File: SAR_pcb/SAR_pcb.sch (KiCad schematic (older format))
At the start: 41 parts, among them J1 Conn_Coaxial_Power, J10 Conn_Coaxial, J11 Conn_Coaxial, J12 Conn_01x02, J13 Conn_01x02, J14 Conn_01x02, J15 Conn_01x02, J16 Conn_01x02, J17 Conn_01x02, J18 Conn_01x02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

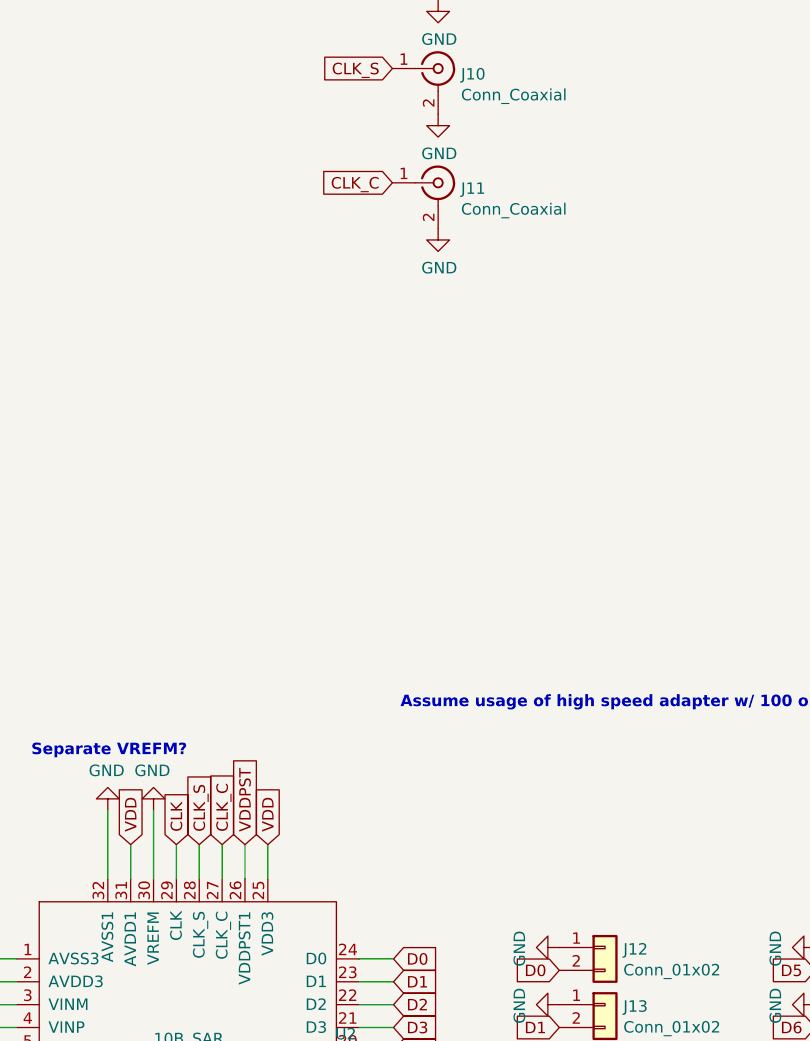
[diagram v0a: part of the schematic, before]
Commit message: Added jumper resistance for feeding clk_c
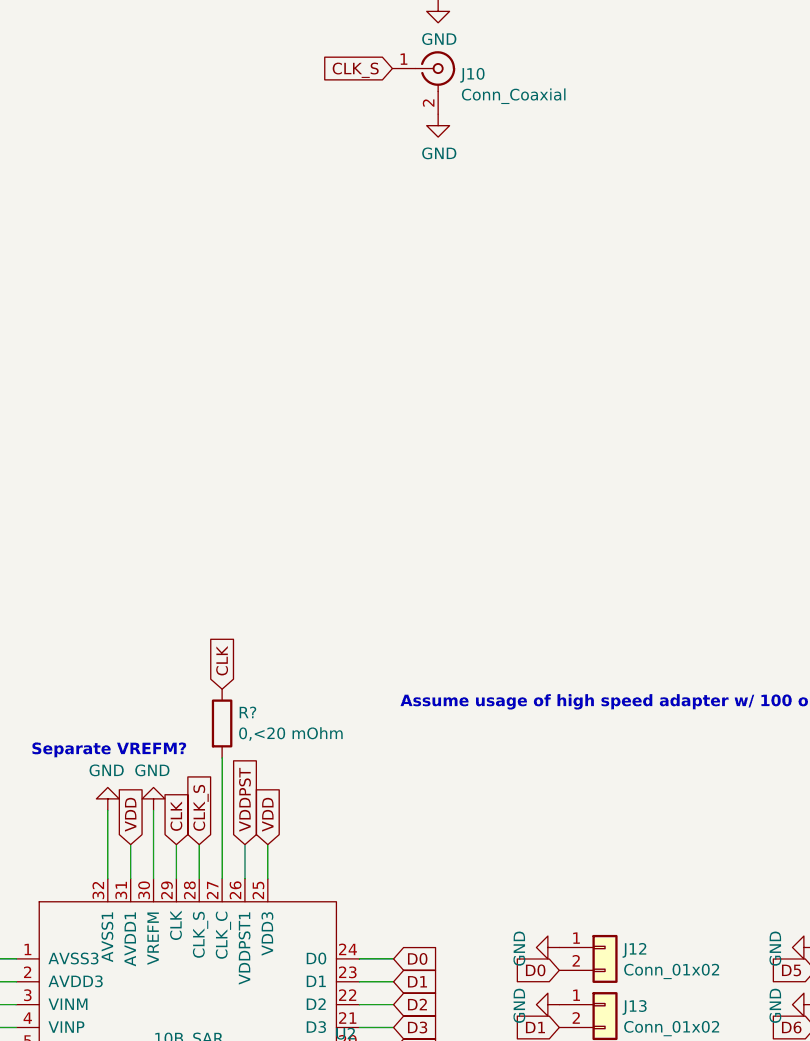
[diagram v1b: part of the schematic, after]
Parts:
- removed J11: Conn_Coaxial, Connector_Coaxial:SMA_Amphenol_132289_EdgeMount, symbol Connector:Conn_Coaxial
- added R?: 0,<20 mOhm, Resistor_SMD:R_0805_2012Metric, symbol Device:R
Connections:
- net CLK: now also R?.1
- net CLK_C: no longer names the net of U2.27 (CLK_C)
- net CLK_C: now also R?.2
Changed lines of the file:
@@
 Comment4 ""
 $EndDescr
-Text GLabel 6005 4745 1    50   Input ~ 0
-CLK_C
 Text GLabel 6105 4745 1    50   Input ~ 0
 VDDPST
@@
 	6105 4895 6105 4745
 Wire Wire Line
-	6005 4895 6005 4745
-Wire Wire Line
 	5905 4895 5905 4745
 Wire Wire Line
@@
 $EndComp
 $Comp
-L Connector:Conn_Coaxial J11
-U 1 1 5F7C18E6
-P 6950 1850
-F 0 "J11" H 7050 1825 50  0000 L CNN
-F 1 "Conn_Coaxial" H 7050 1734 50  0000 L CNN
-F 2 "Connector_Coaxial:SMA_Amphenol_132289_EdgeMount" H 6950 1850 50  0001 C CNN
-F 3 " ~" H 6950 1850 50  0001 C CNN
-	1    6950 1850
-	1    0    0    -1
-$EndComp
-$Comp
 L Connector:Conn_Coaxial J9
 U 1 1 5F7C2E44
@@
 $EndComp
 $Comp
-L power:GND #PWR019
-U 1 1 5F7C5123
-P 6950 2050
-F 0 "#PWR019" H 6950 1800 50  0001 C CNN
-F 1 "GND" H 6955 1877 50  0000 C CNN
-F 2 "" H 6950 2050 50  0001 C CNN
-F 3 "" H 6950 2050 50  0001 C CNN
-	1    6950 2050
-	1    0    0    -1
-$EndComp
-$Comp
 L power:GND #PWR018
 U 1 1 5F7C6414
@@
 	1    0    0    -1
 $EndComp
-Text GLabel 6750 1850 0    50   Input ~ 0
-CLK_C
 Text GLabel 6750 1350 0    50   Input ~ 0
 CLK_S
@@
 EndData
 $EndBitmap
+Text GLabel 6005 4065 1    50   Input ~ 0
+CLK
+$Comp
+L Device:R R?
+U 1 1 5F8560B6
+P 6005 4215
+F 0 "R?" H 6075 4261 50  0000 L CNN
+F 1 "0,<20 mOhm" H 6075 4170 50  0000 L CNN
+F 2 "Resistor_SMD:R_0805_2012Metric" V 5935 4215 50  0001 C CNN
+F 3 "https://www.digikey.com/short/znt8qf" H 6005 4215 50  0001 C CNN
+	1    6005 4215
+	1    0    0    -1
+$EndComp
+Wire Wire Line
+	6005 4365 6005 4895
 $EndSCHEMATC

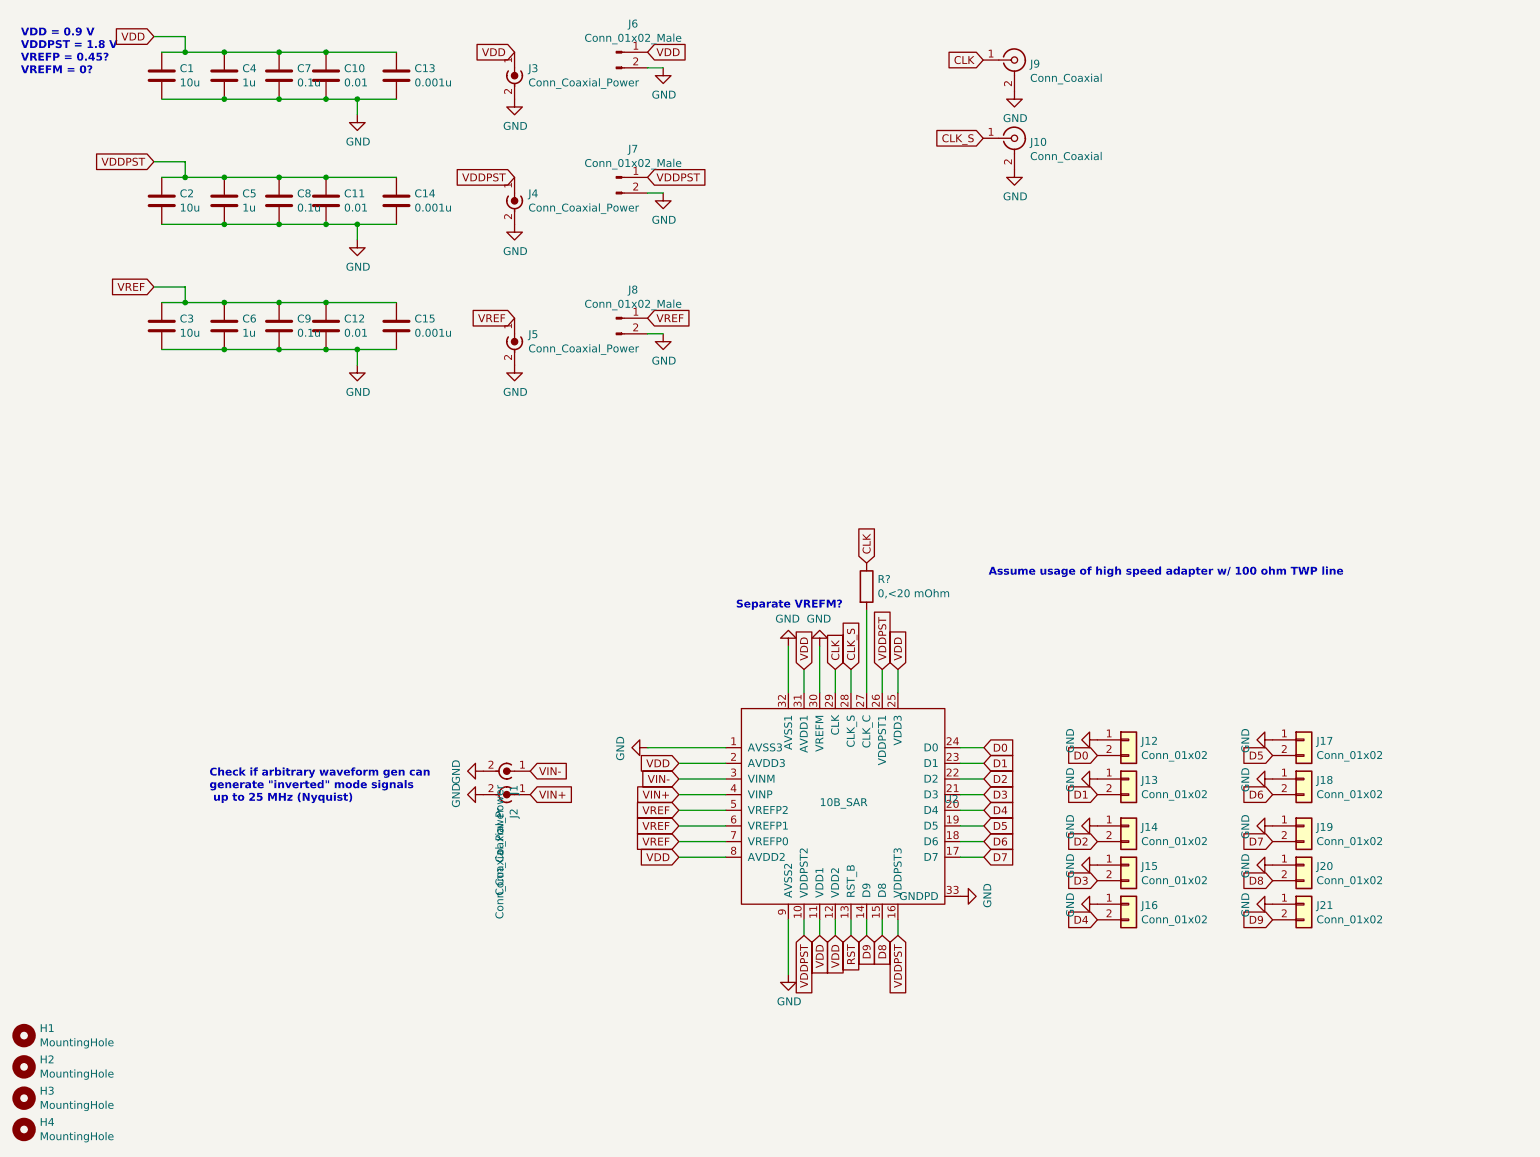
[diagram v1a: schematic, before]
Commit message: Finalized clock terminations, did BOM, TODO: BOM for input elements (see box)
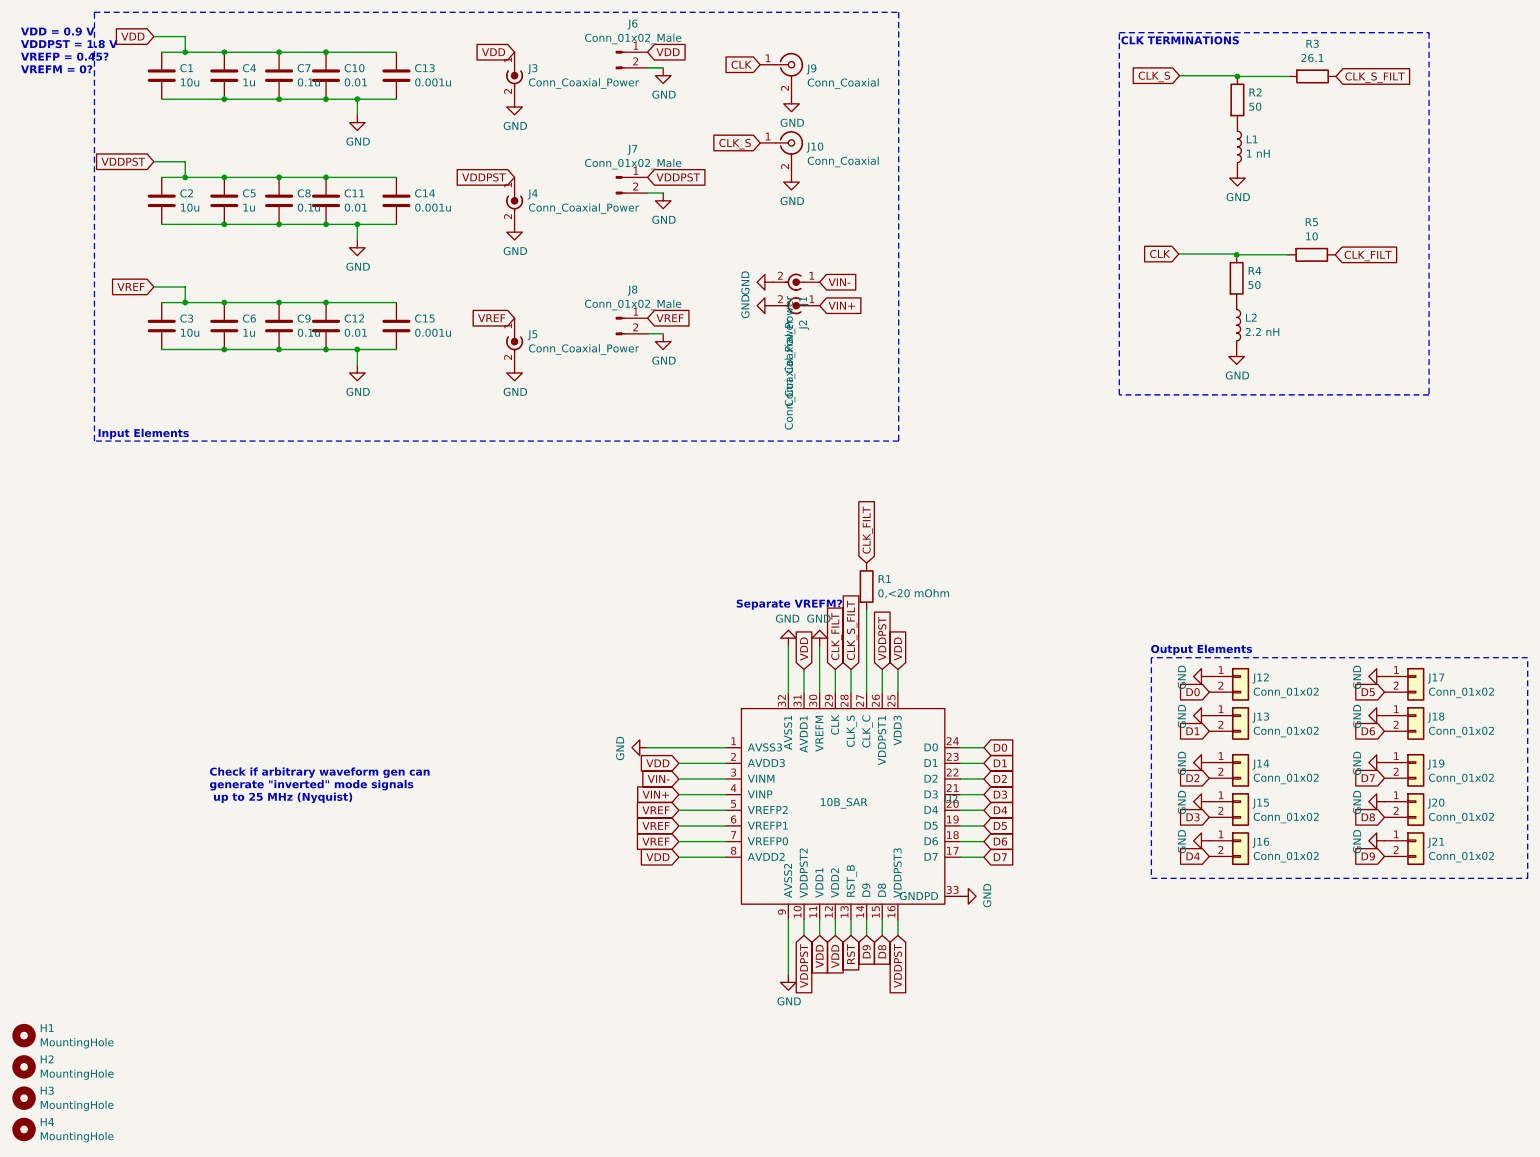
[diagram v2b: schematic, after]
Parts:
- added L1: 1 nH, Inductor_SMD:L_0603_1608Metric, symbol Device:L
- added L2: 2.2 nH, Inductor_SMD:L_0805_2012Metric, symbol Device:L
- added R2, R4: 50, Resistor_SMD:R_0805_2012Metric, symbol Device:R
- added R3: 26.1, Resistor_SMD:R_0805_2012Metric, symbol Device:R
- added R5: 10, Resistor_SMD:R_0805_2012Metric, symbol Device:R
- gave numbers to parts that had none: 1
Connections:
- net CLK: now also R4.1, R5.2; no longer R1.1, U2.29 (CLK)
- net CLK_S: now also R2.1, R3.2; no longer U2.28 (CLK_S)
- net GND: now also L1.2, L2.2
- new net: L1.1, R2.2
- new net: L2.1, R4.2
- new net CLK_FILT: R1.1, R5.1, U2.29 (CLK)
- new net CLK_S_FILT: R3.1, U2.28 (CLK_S)
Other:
- note added: "CLK TERMINATIONS"
- note added: "Input Elements"
- note added: "Output Elements"
- note removed: "Assume usage of high speed adapter w/ 100 ohm TWP line"
- moved on the sheet: J1, J10, J12, J13, J14, J15, J16, J17, J18, J19, J2, J20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

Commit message: Updated footprints from 0805 handsolder to regular 0805
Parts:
- C1, C10, C11, C12, C13, C14, C15, C2, C3, C4, C5, C6, C7, C8, C9: footprint Capacitor_SMD:C_0805_2012Metric_Pad1.15x1.40mm_HandSolder -> Capacitor_SMD:C_0805_2012Metric
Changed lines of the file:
@@
 F 0 "C13" H 3115 996 50  0000 L CNN
 F 1 "0.001u" H 3115 905 50  0000 L CNN
-F 2 "Capacitor_SMD:C_0805_2012Metric_Pad1.15x1.40mm_HandSolder" H 3038 800 50  0001 C CNN
+F 2 "Capacitor_SMD:C_0805_2012Metric" H 3038 800 50  0001 C CNN
 F 3 "~" H 3000 950 50  0001 C CNN
 	1    3000 950
@@
 F 0 "C10" H 2665 996 50  0000 L CNN
 F 1 "0.01" H 2665 905 50  0000 L CNN
-F 2 "Capacitor_SMD:C_0805_2012Metric_Pad1.15x1.40mm_HandSolder" H 2588 800 50  0001 C CNN
+F 2 "Capacitor_SMD:C_0805_2012Metric" H 2588 800 50  0001 C CNN
 F 3 "~" H 2550 950 50  0001 C CNN
 	1    2550 950
@@
 F 0 "C7" H 2365 996 50  0000 L CNN
 F 1 "0.1u" H 2365 905 50  0000 L CNN
-F 2 "Capacitor_SMD:C_0805_2012Metric_Pad1.15x1.40mm_HandSolder" H 2288 800 50  0001 C CNN
+F 2 "Capacitor_SMD:C_0805_2012Metric" H 2288 800 50  0001 C CNN
 F 3 "~" H 2250 950 50  0001 C CNN
 	1    2250 950
@@
 F 0 "C4" H 2015 996 50  0000 L CNN
 F 1 "1u" H 2015 905 50  0000 L CNN
-F 2 "Capacitor_SMD:C_0805_2012Metric_Pad1.15x1.40mm_HandSolder" H 1938 800 50  0001 C CNN
+F 2 "Capacitor_SMD:C_0805_2012Metric" H 1938 800 50  0001 C CNN
 F 3 "~" H 1900 950 50  0001 C CNN
 	1    1900 950
@@
 F 0 "C1" H 1615 996 50  0000 L CNN
 F 1 "10u" H 1615 905 50  0000 L CNN
-F 2 "Capacitor_SMD:C_0805_2012Metric_Pad1.15x1.40mm_HandSolder" H 1538 800 50  0001 C CNN
+F 2 "Capacitor_SMD:C_0805_2012Metric" H 1538 800 50  0001 C CNN
 F 3 "~" H 1500 950 50  0001 C CNN
 	1    1500 950
@@
 F 0 "C14" H 3115 1796 50  0000 L CNN
 F 1 "0.001u" H 3115 1705 50  0000 L CNN
-F 2 "Capacitor_SMD:C_0805_2012Metric_Pad1.15x1.40mm_HandSolder" H 3038 1600 50  0001 C CNN
+F 2 "Capacitor_SMD:C_0805_2012Metric" H 3038 1600 50  0001 C CNN
 F 3 "~" H 3000 1750 50  0001 C CNN
 	1    3000 1750
@@
 F 0 "C11" H 2665 1796 50  0000 L CNN
 F 1 "0.01" H 2665 1705 50  0000 L CNN
-F 2 "Capacitor_SMD:C_0805_2012Metric_Pad1.15x1.40mm_HandSolder" H 2588 1600 50  0001 C CNN
+F 2 "Capacitor_SMD:C_0805_2012Metric" H 2588 1600 50  0001 C CNN
 F 3 "~" H 2550 1750 50  0001 C CNN
 	1    2550 1750
@@
 F 0 "C8" H 2365 1796 50  0000 L CNN
 F 1 "0.1u" H 2365 1705 50  0000 L CNN
-F 2 "Capacitor_SMD:C_0805_2012Metric_Pad1.15x1.40mm_HandSolder" H 2288 1600 50  0001 C CNN
+F 2 "Capacitor_SMD:C_0805_2012Metric" H 2288 1600 50  0001 C CNN
 F 3 "~" H 2250 1750 50  0001 C CNN
 	1    2250 1750
@@
 F 0 "C5" H 2015 1796 50  0000 L CNN
 F 1 "1u" H 2015 1705 50  0000 L CNN
-F 2 "Capacitor_SMD:C_0805_2012Metric_Pad1.15x1.40mm_HandSolder" H 1938 1600 50  0001 C CNN
+F 2 "Capacitor_SMD:C_0805_2012Metric" H 1938 1600 50  0001 C CNN
 F 3 "~" H 1900 1750 50  0001 C CNN
 	1    1900 1750
@@
 F 0 "C2" H 1615 1796 50  0000 L CNN
 F 1 "10u" H 1615 1705 50  0000 L CNN
-F 2 "Capacitor_SMD:C_0805_2012Metric_Pad1.15x1.40mm_HandSolder" H 1538 1600 50  0001 C CNN
+F 2 "Capacitor_SMD:C_0805_2012Metric" H 1538 1600 50  0001 C CNN
 F 3 "~" H 1500 1750 50  0001 C CNN
 	1    1500 1750
@@
 F 0 "C15" H 3115 2596 50  0000 L CNN
 F 1 "0.001u" H 3115 2505 50  0000 L CNN
-F 2 "Capacitor_SMD:C_0805_2012Metric_Pad1.15x1.40mm_HandSolder" H 3038 2400 50  0001 C CNN
+F 2 "Capacitor_SMD:C_0805_2012Metric" H 3038 2400 50  0001 C CNN
 F 3 "~" H 3000 2550 50  0001 C CNN
 	1    3000 2550
@@
 F 0 "C12" H 2665 2596 50  0000 L CNN
 F 1 "0.01" H 2665 2505 50  0000 L CNN
-F 2 "Capacitor_SMD:C_0805_2012Metric_Pad1.15x1.40mm_HandSolder" H 2588 2400 50  0001 C CNN
+F 2 "Capacitor_SMD:C_0805_2012Metric" H 2588 2400 50  0001 C CNN
 F 3 "~" H 2550 2550 50  0001 C CNN
 	1    2550 2550
@@
 F 0 "C9" H 2365 2596 50  0000 L CNN
 F 1 "0.1u" H 2365 2505 50  0000 L CNN
-F 2 "Capacitor_SMD:C_0805_2012Metric_Pad1.15x1.40mm_HandSolder" H 2288 2400 50  0001 C CNN
+F 2 "Capacitor_SMD:C_0805_2012Metric" H 2288 2400 50  0001 C CNN
 F 3 "~" H 2250 2550 50  0001 C CNN
 	1    2250 2550
@@
 F 0 "C6" H 2015 2596 50  0000 L CNN
 F 1 "1u" H 2015 2505 50  0000 L CNN
-F 2 "Capacitor_SMD:C_0805_2012Metric_Pad1.15x1.40mm_HandSolder" H 1938 2400 50  0001 C CNN
+F 2 "Capacitor_SMD:C_0805_2012Metric" H 1938 2400 50  0001 C CNN
 F 3 "~" H 1900 2550 50  0001 C CNN
 	1    1900 2550
@@
 F 0 "C3" H 1615 2596 50  0000 L CNN
 F 1 "10u" H 1615 2505 50  0000 L CNN
-F 2 "Capacitor_SMD:C_0805_2012Metric_Pad1.15x1.40mm_HandSolder" H 1538 2400 50  0001 C CNN
+F 2 "Capacitor_SMD:C_0805_2012Metric" H 1538 2400 50  0001 C CNN
 F 3 "~" H 1500 2550 50  0001 C CNN
 	1    1500 2550
